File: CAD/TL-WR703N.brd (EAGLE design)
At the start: 48.5 x 50.1 mm, 241 parts, among them T1 H1601CG, U1 AR9331-AL1A, U2 A3S56F40FTP

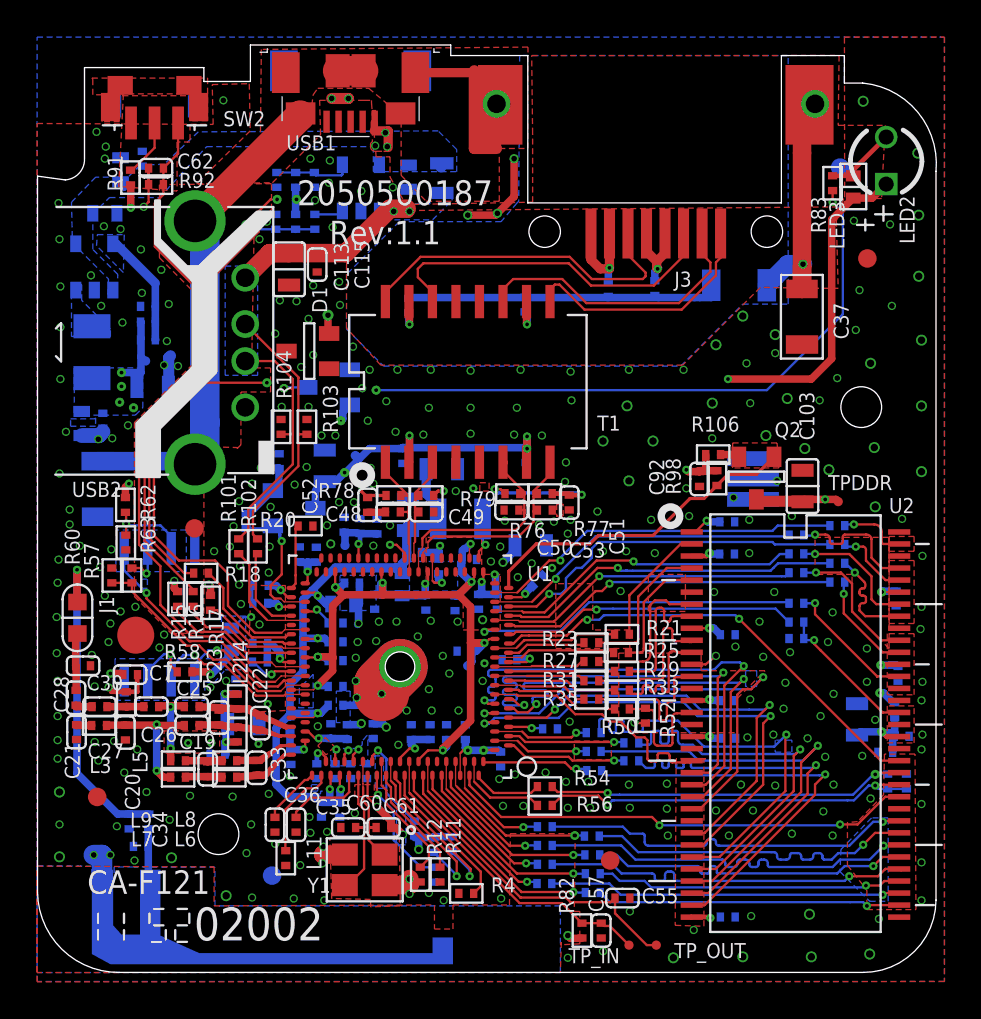
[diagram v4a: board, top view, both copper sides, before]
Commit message: Connected a few missing pads to GND
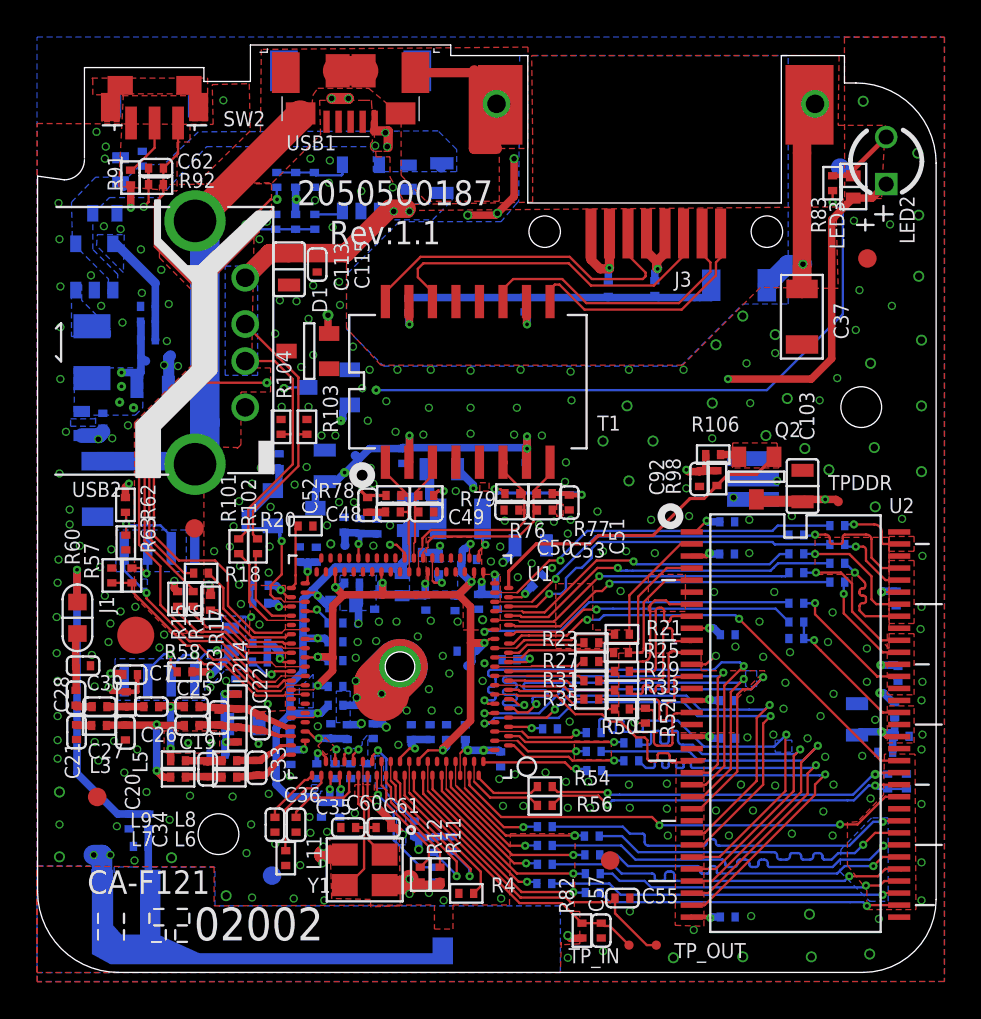
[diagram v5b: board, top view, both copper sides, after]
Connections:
- new net S$45: C38.2
- net GND: now also R11.1, R12.1, R63.2
- net S$113: now also R112.1
- net S$171: now also R2.2
- net VDD: now also C10.2
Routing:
- net S$45: track 0.00 -> 1.38 mm
- net GND: track 35.8 -> 37.1 mm
- net S$113: track 24.5 -> 25.2 mm
- net VDD: track 4.55 -> 5.11 mm
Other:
- outline, holes or cut-outs redrawn
